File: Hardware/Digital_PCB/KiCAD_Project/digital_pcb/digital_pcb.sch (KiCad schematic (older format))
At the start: 28 parts, among them J1 ISP, J2 Board to Board, J3 Conn_01x02, J4 Spare 1, J7 Conn_01x02, U1 STM32F103CBTx, Y1 8MHz

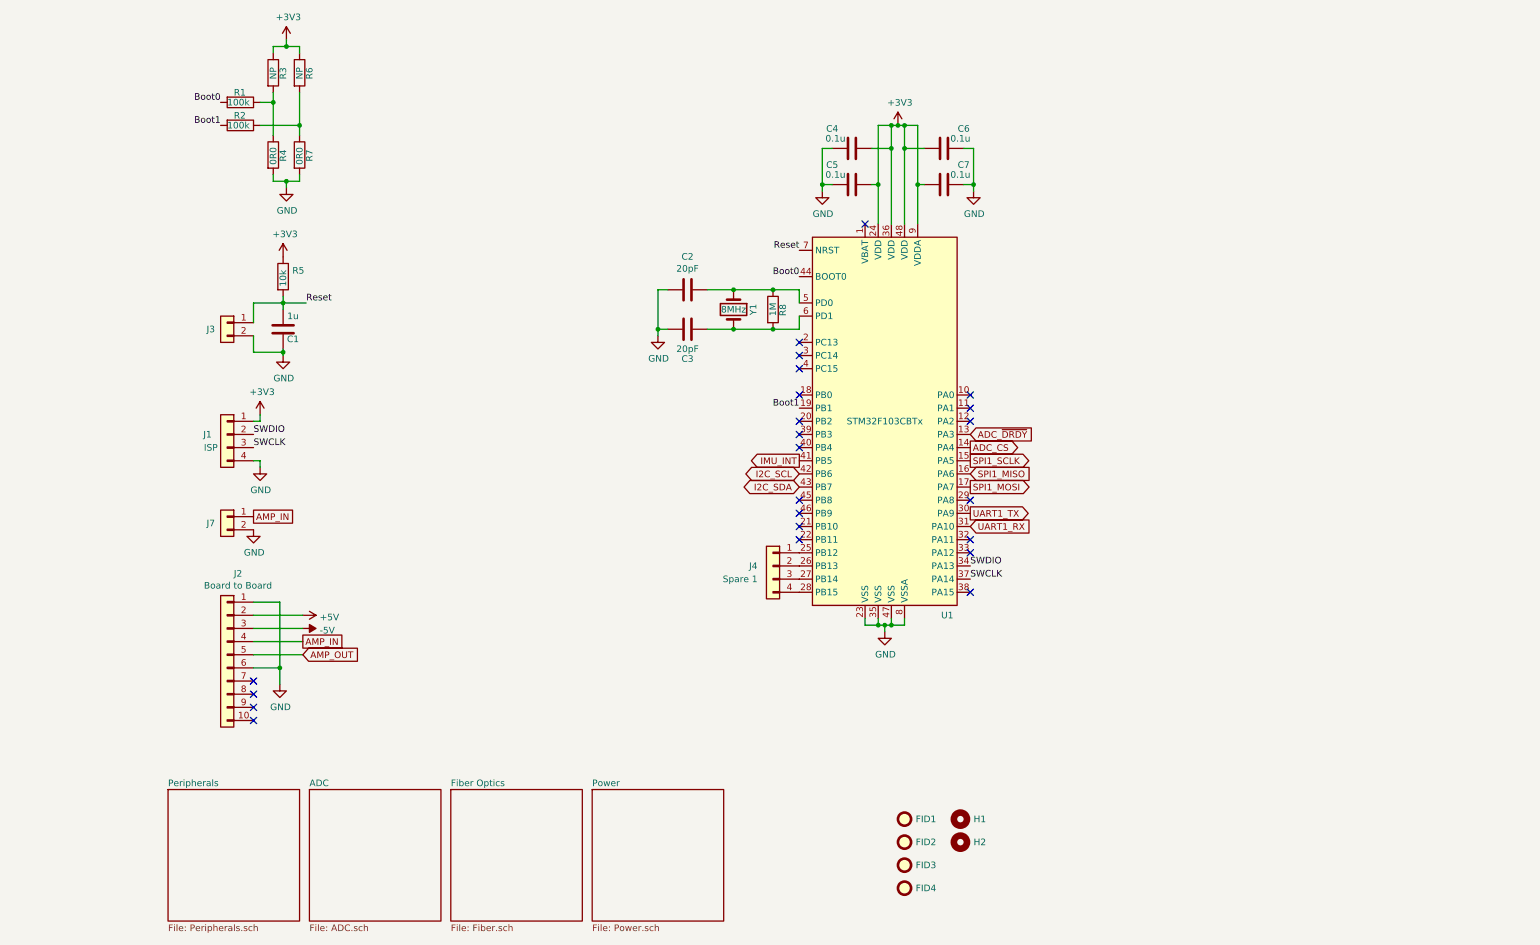
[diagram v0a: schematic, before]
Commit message: Add pullups and divider for ADC input.
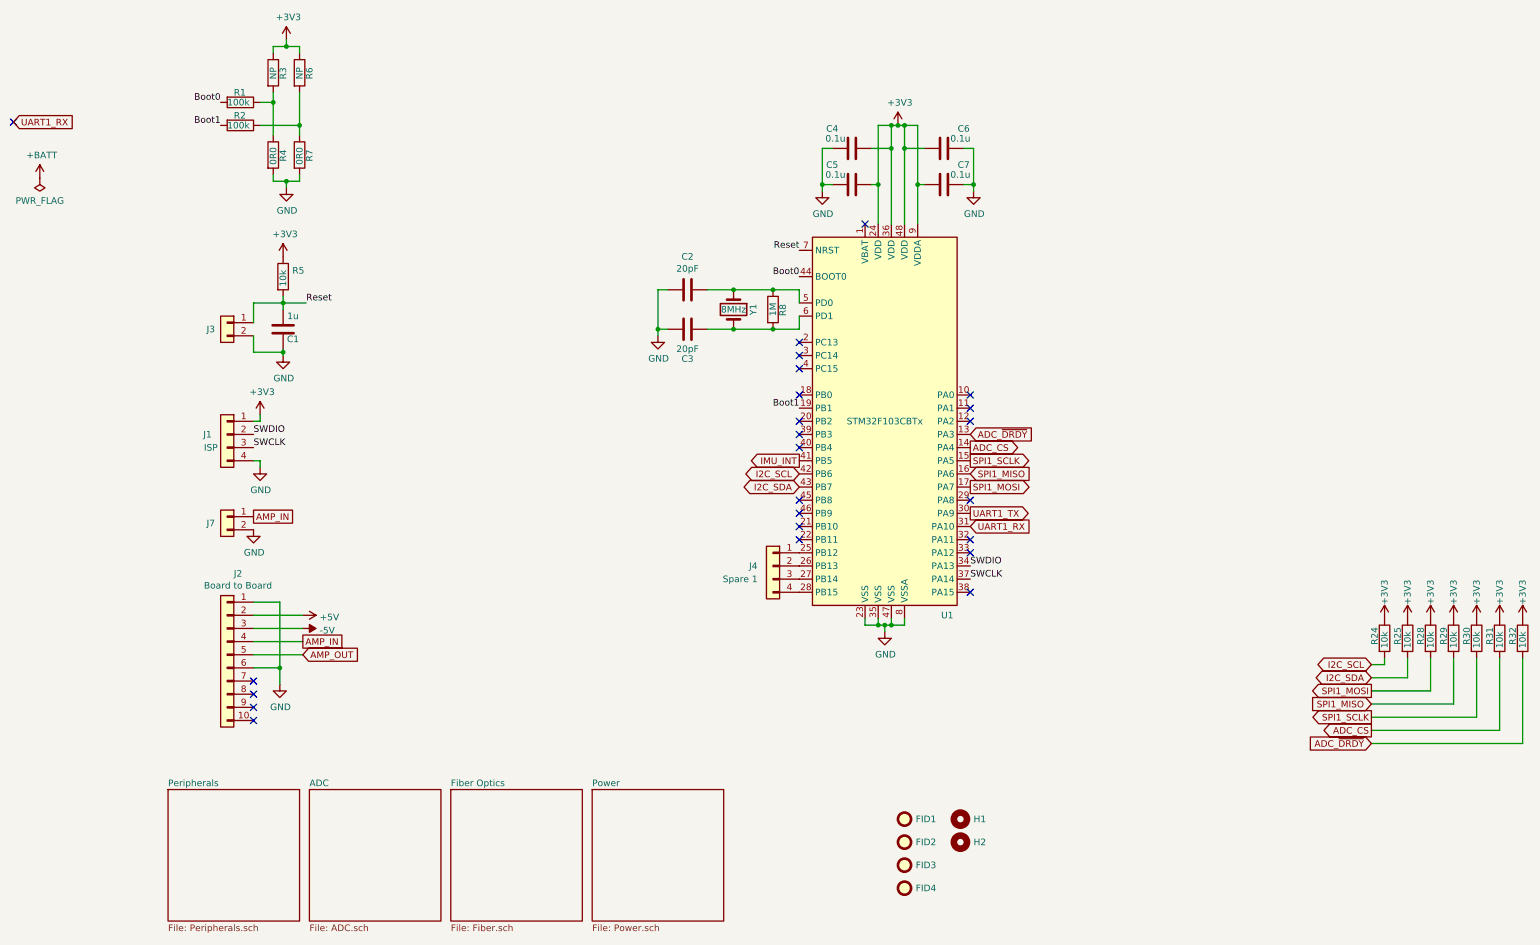
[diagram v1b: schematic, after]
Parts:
- added R24, R25, R28, R29, R30, R31, R32: 10k, Resistors_SMD:R_0603_HandSoldering, symbol Device:R
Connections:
- net +3V3: now also R24.1, R25.1, R28.1, R29.1, R30.1, R31.1, R32.1
- net ADC_CS: now also R31.2
- net ADC_~DRDY: now also R32.2
- net I2C_SCL: now also R24.2
- net I2C_SDA: now also R25.2
- net SPI1_MISO: now also R29.2
- net SPI1_MOSI: now also R28.2
- net SPI1_SCLK: now also R30.2
- no-connect marks 23 -> 24
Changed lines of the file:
@@
 	1    0    0    -1
 $EndComp
+Text GLabel -600 1600 2    50   Input ~ 0
+UART1_RX
+$Comp
+L power:+BATT #PWR0101
+U 1 1 5E0D98E4
+P -400 2025
+F 0 "#PWR0101" H -400 1875 50  0001 C CNN
+F 1 "+BATT" H -385 2198 50  0000 C CNN
+F 2 "" H -400 2025 50  0001 C CNN
+F 3 "" H -400 2025 50  0001 C CNN
+	1    -400 2025
+	1    0    0    -1
+$EndComp
+$Comp
+L power:PWR_FLAG #FLG0101
+U 1 1 5E0D9D35
+P -400 2025
+F 0 "#FLG0101" H -400 2100 50  0001 C CNN
+F 1 "PWR_FLAG" H -400 2198 50  0000 C CNN
+F 2 "" H -400 2025 50  0001 C CNN
+F 3 "~" H -400 2025 50  0001 C CNN
+	1    -400 2025
+	-1   0    0    1
+$EndComp
+NoConn ~ -600 1600
+Text GLabel 9725 5825 0    50   BiDi ~ 0
+I2C_SDA
+Text GLabel 9725 5725 0    50   BiDi ~ 0
+I2C_SCL
+$Comp
+L Device:R R24
+U 1 1 5E0E3EE7
+P 9825 5525
+F 0 "R24" V 9750 5475 50  0000 L CNN
+F 1 "10k" V 9825 5450 50  0000 L CNN
+F 2 "Resistors_SMD:R_0603_HandSoldering" V 9755 5525 50  0001 C CNN
+F 3 "~" H 9825 5525 50  0001 C CNN
+F 4 "1-0000010" H 9825 5525 50  0001 C CNN "Internal Part Number"
+F 5 "1" H 9825 5525 50  0001 C CNN "Populated"
+	1    9825 5525
+	1    0    0    -1
+$EndComp
+$Comp
+L Device:R R25
+U 1 1 5E0E4A30
+P 10000 5525
+F 0 "R25" V 9925 5475 50  0000 L CNN
+F 1 "10k" V 10000 5450 50  0000 L CNN
+F 2 "Resistors_SMD:R_0603_HandSoldering" V 9930 5525 50  0001 C CNN
+F 3 "~" H 10000 5525 50  0001 C CNN
+F 4 "1-0000010" H 10000 5525 50  0001 C CNN "Internal Part Number"
+F 5 "1" H 10000 5525 50  0001 C CNN "Populated"
+	1    10000 5525
+	1    0    0    -1
+$EndComp
+Wire Wire Line
+	9725 5725 9825 5725
+Wire Wire Line
+	9825 5725 9825 5675
+Wire Wire Line
+	9725 5825 10000 5825
+Wire Wire Line
+	10000 5825 10000 5675
+$Comp
+L power:+3V3 #PWR080
+U 1 1 5E0E974F
+P 9825 5375
+F 0 "#PWR080" H 9825 5225 50  0001 C CNN
+F 1 "+3V3" V 9825 5575 50  0000 C CNN
+F 2 "" H 9825 5375 50  0001 C CNN
+F 3 "" H 9825 5375 50  0001 C CNN
+	1    9825 5375
+	1    0    0    -1
+$EndComp
+$Comp
+L power:+3V3 #PWR081
+U 1 1 5E0EA302
+P 10000 5375
+F 0 "#PWR081" H 10000 5225 50  0001 C CNN
+F 1 "+3V3" V 10000 5575 50  0000 C CNN
+F 2 "" H 10000 5375 50  0001 C CNN
+F 3 "" H 10000 5375 50  0001 C CNN
+	1    10000 5375
+	1    0    0    -1
+$EndComp
+Text GLabel 9725 6225 0    50   Output ~ 0
+ADC_CS
+Text GLabel 9725 6125 0    50   Output ~ 0
+SPI1_SCLK
+Text GLabel 9725 5925 0    50   Output ~ 0
+SPI1_MOSI
+Text GLabel 9725 6025 0    50   Input ~ 0
+SPI1_MISO
+Text GLabel 9725 6325 0    50   Input ~ 0
+ADC_~DRDY
+$Comp
+L Device:R R28
+U 1 1 5E0FBDB5
+P 10175 5525
+F 0 "R28" V 10100 5475 50  0000 L CNN
+F 1 "10k" V 10175 5450 50  0000 L CNN
+F 2 "Resistors_SMD:R_0603_HandSoldering" V 10105 5525 50  0001 C CNN
+F 3 "~" H 10175 5525 50  0001 C CNN
+F 4 "1-0000010" H 10175 5525 50  0001 C CNN "Internal Part Number"
+F 5 "1" H 10175 5525 50  0001 C CNN "Populated"
+	1    10175 5525
+	1    0    0    -1
+$EndComp
+$Comp
+L Device:R R29
+U 1 1 5E0FBDBD
+P 10350 5525
+F 0 "R29" V 10275 5475 50  0000 L CNN
+F 1 "10k" V 10350 5450 50  0000 L CNN
+F 2 "Resistors_SMD:R_0603_HandSoldering" V 10280 5525 50  0001 C CNN
+F 3 "~" H 10350 5525 50  0001 C CNN
+F 4 "1-0000010" H 10350 5525 50  0001 C CNN "Internal Part Number"
+F 5 "1" H 10350 5525 50  0001 C CNN "Populated"
+	1    10350 5525
+	1    0    0    -1
+$EndComp
+$Comp
+L power:+3V3 #PWR0102
+U 1 1 5E0FBDC3
+P 10175 5375
+F 0 "#PWR0102" H 10175 5225 50  0001 C CNN
+F 1 "+3V3" V 10175 5575 50  0000 C CNN
+F 2 "" H 10175 5375 50  0001 C CNN
+F 3 "" H 10175 5375 50  0001 C CNN
+	1    10175 5375
+	1    0    0    -1
+$EndComp
+$Comp
+L power:+3V3 #PWR0103
+U 1 1 5E0FBDC9
+P 10350 5375
+F 0 "#PWR0103" H 10350 5225 50  0001 C CNN
+F 1 "+3V3" V 10350 5575 50  0000 C CNN
+F 2 "" H 10350 5375 50  0001 C CNN
+F 3 "" H 10350 5375 50  0001 C CNN
+	1    10350 5375
+	1    0    0    -1
+$EndComp
+$Comp
+L Device:R R30
+U 1 1 5E0FEE7E
+P 10525 5525
+F 0 "R30" V 10450 5475 50  0000 L CNN
+F 1 "10k" V 10525 5450 50  0000 L CNN
+F 2 "Resistors_SMD:R_0603_HandSoldering" V 10455 5525 50  0001 C CNN
+F 3 "~" H 10525 5525 50  0001 C CNN
+F 4 "1-0000010" H 10525 5525 50  0001 C CNN "Internal Part Number"
+F 5 "1" H 10525 5525 50  0001 C CNN "Populated"
+	1    10525 5525
+	1    0    0    -1
+$EndComp
+$Comp
+L Device:R R31
+U 1 1 5E0FEE86
+P 10700 5525
+F 0 "R31" V 10625 5475 50  0000 L CNN
+F 1 "10k" V 10700 5450 50  0000 L CNN
+F 2 "Resistors_SMD:R_0603_HandSoldering" V 10630 5525 50  0001 C CNN
+F 3 "~" H 10700 5525 50  0001 C CNN
+F 4 "1-0000010" H 10700 5525 50  0001 C CNN "Internal Part Number"
+F 5 "1" H 10700 5525 50  0001 C CNN "Populated"
+	1    10700 5525
+	1    0    0    -1
+$EndComp
+$Comp
+L power:+3V3 #PWR0104
+U 1 1 5E0FEE8C
+P 10525 5375
+F 0 "#PWR0104" H 10525 5225 50  0001 C CNN
+F 1 "+3V3" V 10525 5575 50  0000 C CNN
+F 2 "" H 10525 5375 50  0001 C CNN
+F 3 "" H 10525 5375 50  0001 C CNN
+	1    10525 5375
+	1    0    0    -1
+$EndComp
+$Comp
+L power:+3V3 #PWR0105
+U 1 1 5E0FEE92
+P 10700 5375
+F 0 "#PWR0105" H 10700 5225 50  0001 C CNN
+F 1 "+3V3" V 10700 5575 50  0000 C CNN
+F 2 "" H 10700 5375 50  0001 C CNN
+F 3 "" H 10700 5375 50  0001 C CNN
+	1    10700 5375
+	1    0    0    -1
+$EndComp
+$Comp
+L Device:R R32
+U 1 1 5E1020DD
+P 10875 5525
+F 0 "R32" V 10800 5475 50  0000 L CNN
+F 1 "10k" V 10875 5450 50  0000 L CNN
+F 2 "Resistors_SMD:R_0603_HandSoldering" V 10805 5525 50  0001 C CNN
+F 3 "~" H 10875 5525 50  0001 C CNN
+F 4 "1-0000010" H 10875 5525 50  0001 C CNN "Internal Part Number"
+F 5 "1" H 10875 5525 50  0001 C CNN "Populated"
+	1    10875 5525
+	1    0    0    -1
+$EndComp
+$Comp
+L power:+3V3 #PWR0106
+U 1 1 5E1020EB
+P 10875 5375
+F 0 "#PWR0106" H 10875 5225 50  0001 C CNN
+F 1 "+3V3" V 10875 5575 50  0000 C CNN
+F 2 "" H 10875 5375 50  0001 C CNN
+F 3 "" H 10875 5375 50  0001 C CNN
+	1    10875 5375
+	1    0    0    -1
+$EndComp
+Wire Wire Line
+	9725 5925 10175 5925
+Wire Wire Line
+	10175 5925 10175 5675
+Wire Wire Line
+	9725 6025 10350 6025
+Wire Wire Line
+	10350 6025 10350 5675
+Wire Wire Line
+	9725 6125 10525 6125
+Wire Wire Line
+	10525 6125 10525 5675
+Wire Wire Line
+	9725 6225 10700 6225
+Wire Wire Line
+	10700 6225 10700 5675
+Wire Wire Line
+	9725 6325 10875 6325
+Wire Wire Line
+	10875 6325 10875 5675
 $EndSCHEMATC

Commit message: Digital PCB Rev 1.0 complete.
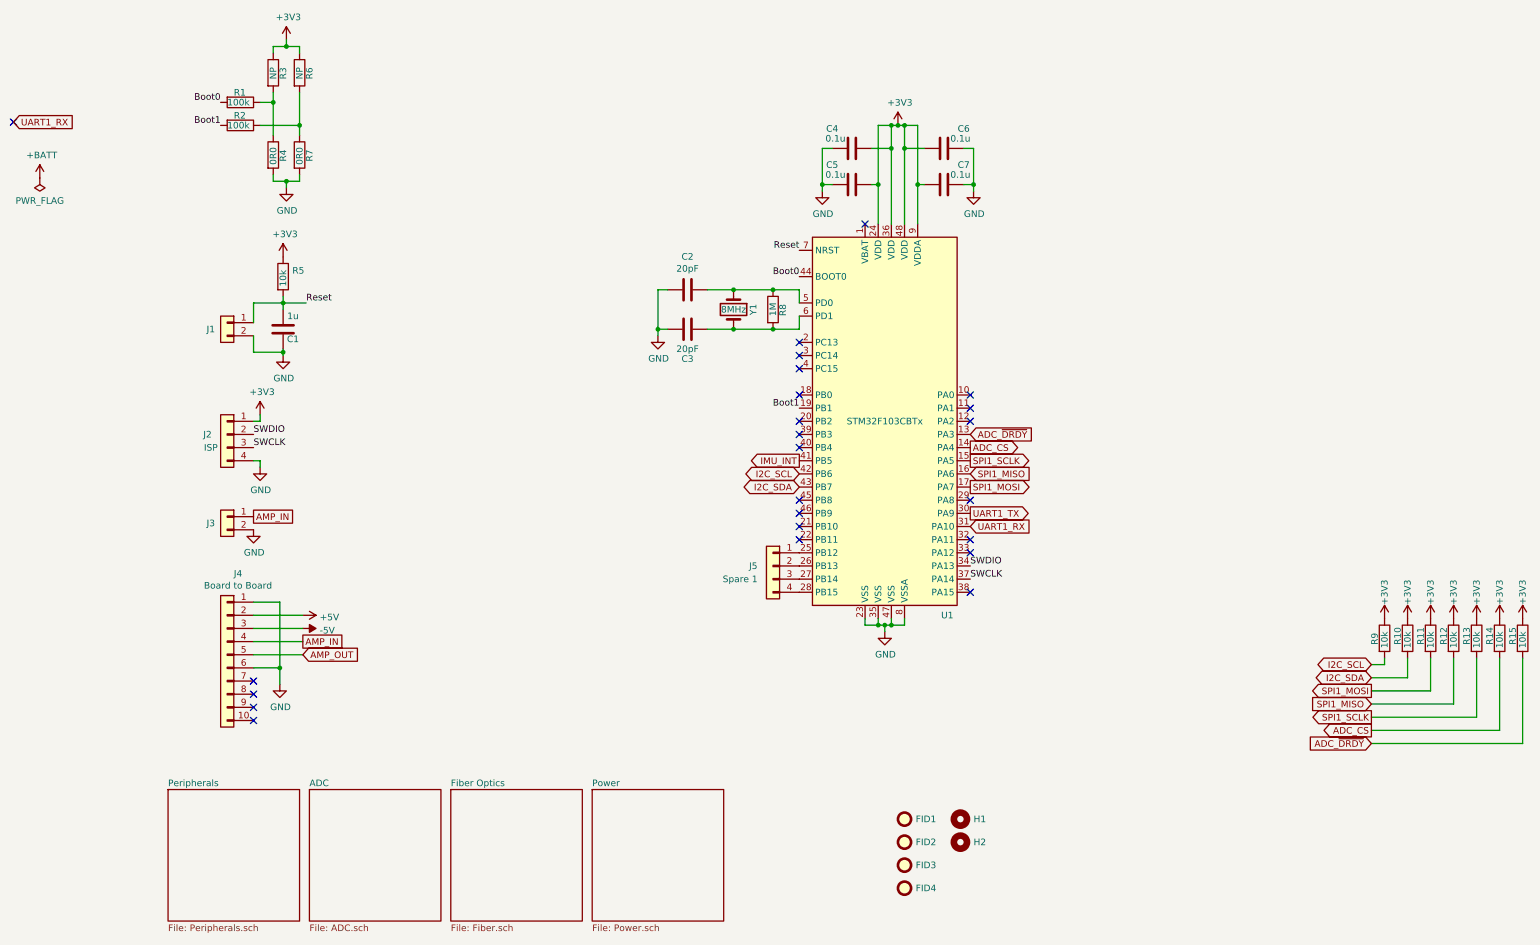
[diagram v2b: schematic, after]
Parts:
- FID1, FID2, FID3, FID4, H1, H2: Internal Part Number (none) -> 0-0000000; Populated (none) -> 0
- renumbered J3 to J1, J1 to J2, J7 to J3, J2 to J4, J4 to J5, R25 to R10, R28 to R11, R29 to R12, R30 to R13, R31 to R14, R32 to R15, R24 to R9

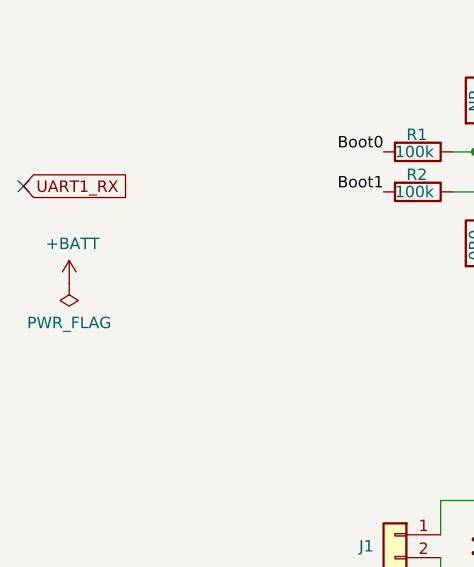
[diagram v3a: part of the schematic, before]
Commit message: Fixup DRC issues.
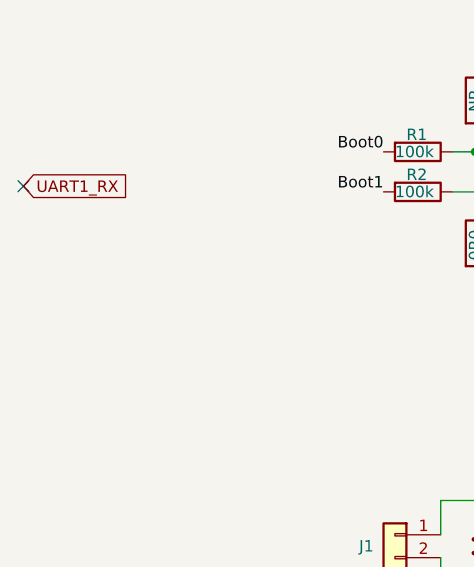
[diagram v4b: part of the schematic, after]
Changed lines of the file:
@@
 Text GLabel -600 1600 2    50   Input ~ 0
 UART1_RX
-$Comp
-L power:+BATT #PWR01
-U 1 1 5E0D98E4
-P -400 2025
-F 0 "#PWR01" H -400 1875 50  0001 C CNN
-F 1 "+BATT" H -385 2198 50  0000 C CNN
-F 2 "" H -400 2025 50  0001 C CNN
-F 3 "" H -400 2025 50  0001 C CNN
-	1    -400 2025
-	1    0    0    -1
-$EndComp
-$Comp
-L power:PWR_FLAG #FLG01
-U 1 1 5E0D9D35
-P -400 2025
-F 0 "#FLG01" H -400 2100 50  0001 C CNN
-F 1 "PWR_FLAG" H -400 2198 50  0000 C CNN
-F 2 "" H -400 2025 50  0001 C CNN
-F 3 "~" H -400 2025 50  0001 C CNN
-	1    -400 2025
-	-1   0    0    1
-$EndComp
 NoConn ~ -600 1600
 Text GLabel 9725 5825 0    50   BiDi ~ 0
